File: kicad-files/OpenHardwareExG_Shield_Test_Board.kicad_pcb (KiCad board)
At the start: 4 copper layers, 125.1 x 59.7 mm, 150 parts, among them P1 CONN_1, P11 CONN_1, P12 CONN_1, P13 CONN_1, P14 CONN_1, P15 CONN_1, P16 CONN_1, P17 CONN_1, P18 CONN_1, P19 ARDUINO_SHIELD, P2 CONN_1, P23 CONN_1, P24 CONN_1, P25 CONN_1, P26 CONN_1, P27 CONN_1, P28 CONN_1, P29 CONN_1, P3 CONN_1, P30 CONN_1, P31 CONN_1, P32 CONN_1, P33 CONN_1, P34 CONN_1, P35 CONN_1, P36 CONN_1, P37 CONN_1, P38 CONN_1, P39 CONN_1, P4 CONN_1, P40 CONN_1, P41 CONN_1, P42 CONN_1, P43 CONN_1, P44 CONN_1, P45 CONN_1, P46 CONN_1, P47 CONN_1, P48 CONN_1, P49 CONN_1, P5 CONN_1, P50 CONN_1, P51 CONN_1, P52 CONN_1, P53 CONN_1, P54 CONN_1, P55 CONN_1, P56 CONN_3X2, P57 CONN_20X2, P6 CONN_1, P7 CONN_1, P8 CONN_1, P9 CONN_1, SW1 SW_PUSH, U1 74HC165, U2 74HC165, U3 74HC595PWR, U4 74HC165, U5 74LS125, U6 TPS2095D, U7 ADUM6000, U8 SI8661

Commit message: untangle the rats nest some
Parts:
- removed R45, R46, R47, R48, R49, R50: 47, SM0603
- moved R34 153.6 mm to (88.3, 55.9), turned to 270 degrees
- moved R39 152.5 mm to (87.6, 60.3), turned to 90 degrees
- moved R37 150.6 mm to (87.6, 64.8), turned to 270 degrees
- moved R36 147.1 mm to (88.3, 51.4), turned to 270 degrees
- moved R35 146.4 mm to (87.6, 68.6), turned to 270 degrees
- moved L1 144.1 mm to (89.5, 71.8), turned to 180 degrees
- moved R14 143.2 mm to (99.7, 62.2), turned to 90 degrees
- moved R12 142.2 mm to (99.7, 66.0), turned to 270 degrees
- moved R9 140.6 mm to (101.0, 52.7)
- moved L2 138.5 mm to (102.9, 71.8), turned to 90 degrees
- moved R11 138.1 mm to (101.0, 50.8)
- moved R13 137.9 mm to (101.0, 48.9)
- moved R15 137.1 mm to (101.0, 47.0)
- moved R10 136.7 mm to (104.8, 66.0)
- moved C5 136.2 mm to (105.4, 71.8), turned to 90 degrees
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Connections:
- net N-000001 renamed /A3
- net N-00000100 renamed /LED2
- net N-00000115 renamed /3.3V_BOGUS_ISO_DATA
- net N-00000132 renamed /LED1
- net N-00000136 renamed /VCC_DATA
- net N-0000018 renamed /A1
- net N-0000019 renamed /A2
- net N-000003 renamed /A4
- net N-0000040 renamed /VISO_BOGUS_ISO_PRE
- net N-0000043 renamed /MIDDLE_CARRY
- net N-0000045 renamed /VDD1
- net N-0000099 renamed /LED3
- U8 pad 11: N-0000020 -> /SHIFT_CLK_BOGUS_ISO
- U8 pad 12: N-0000021 -> /SHIFT_SH_~LD~_BOGUS_ISO
- U8 pad 13: N-0000035 -> /~SEND_TO_GND~_MASTER_BOGUS_ISO
- U8 pad 14: N-0000036 -> /SIGNAL_B_BOGUS_ISO
- U8 pad 15: N-0000022 -> /SIGNAL_A_BOGUS_ISO
- U8 pad 7: N-0000034 -> /SHIFT_CARRY
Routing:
- net /BIASOUT_FILT: track 0.00 -> 119.6 mm
- net /3.3V_BOGUS_ISO: track 0.00 -> 20.6 mm
- net /BIASINV: track 0.00 -> 13.5 mm
- net /SIGNAL_A_LADDER: track 0.00 -> 13.4 mm, vias 0 -> 1
- added copper zone on B.Cu, net GND
- added copper zone on F.Cu, net VCC

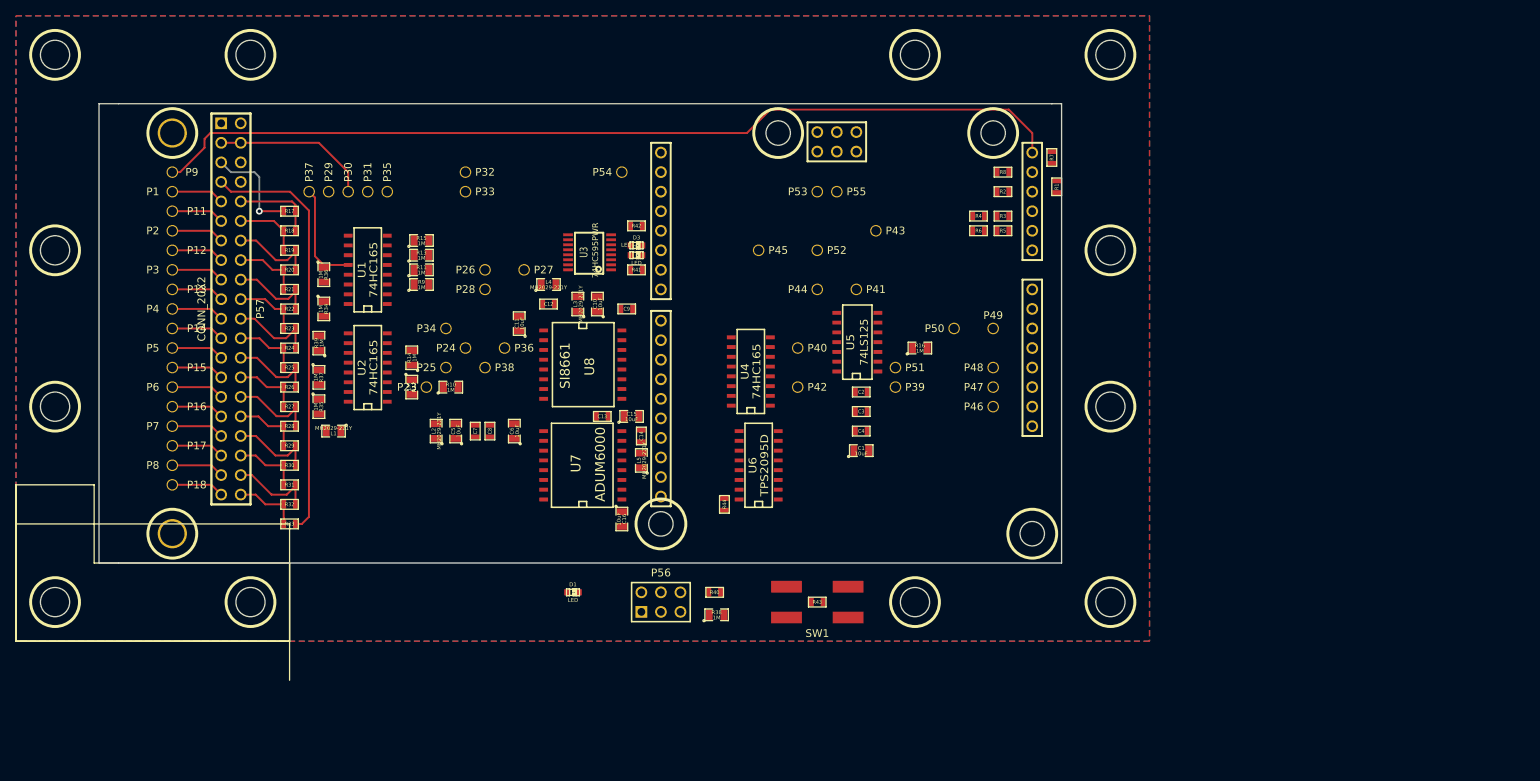
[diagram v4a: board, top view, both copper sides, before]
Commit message: move connectors onto .1 grid
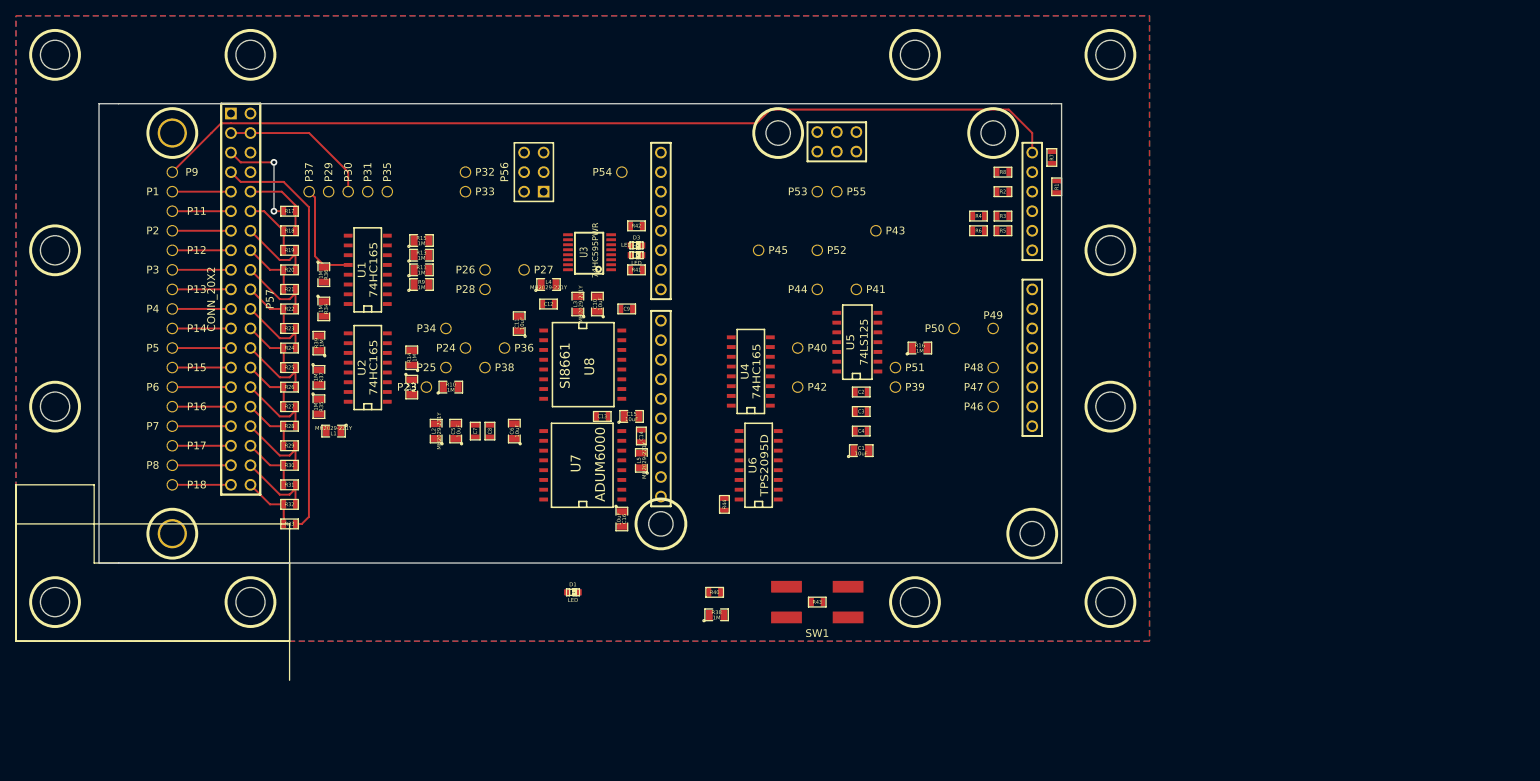
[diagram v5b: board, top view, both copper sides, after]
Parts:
- moved P56 58.3 mm to (115.6, 38.1), turned to 90 degrees
- moved P57 1.80 mm to (77.5, 54.6)
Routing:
- net /IN8N_LADDER: track 10.7 -> 9.88 mm
- net /IN8N: track 6.88 -> 7.62 mm
- net /IN6P_LADDER: track 8.65 -> 7.91 mm
- net /IN6P: track 6.88 -> 7.62 mm
- net /IN5P_LADDER: track 8.65 -> 7.91 mm
- net /IN5P: track 6.88 -> 7.62 mm
- net /IN5N: track 6.88 -> 7.62 mm
- net /IN4P_LADDER: track 8.65 -> 7.91 mm
- net /IN4P: track 6.88 -> 7.62 mm
- net /IN4N: track 6.88 -> 7.62 mm
- net /IN3P_LADDER: track 8.65 -> 7.91 mm
- net /IN3P: track 6.88 -> 7.62 mm
- net /IN3N: track 6.88 -> 7.62 mm
- net /IN2N: track 6.88 -> 7.62 mm
- net /IN1N: track 6.88 -> 7.62 mm
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
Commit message: power chips on isolated side of test harness from the board under test
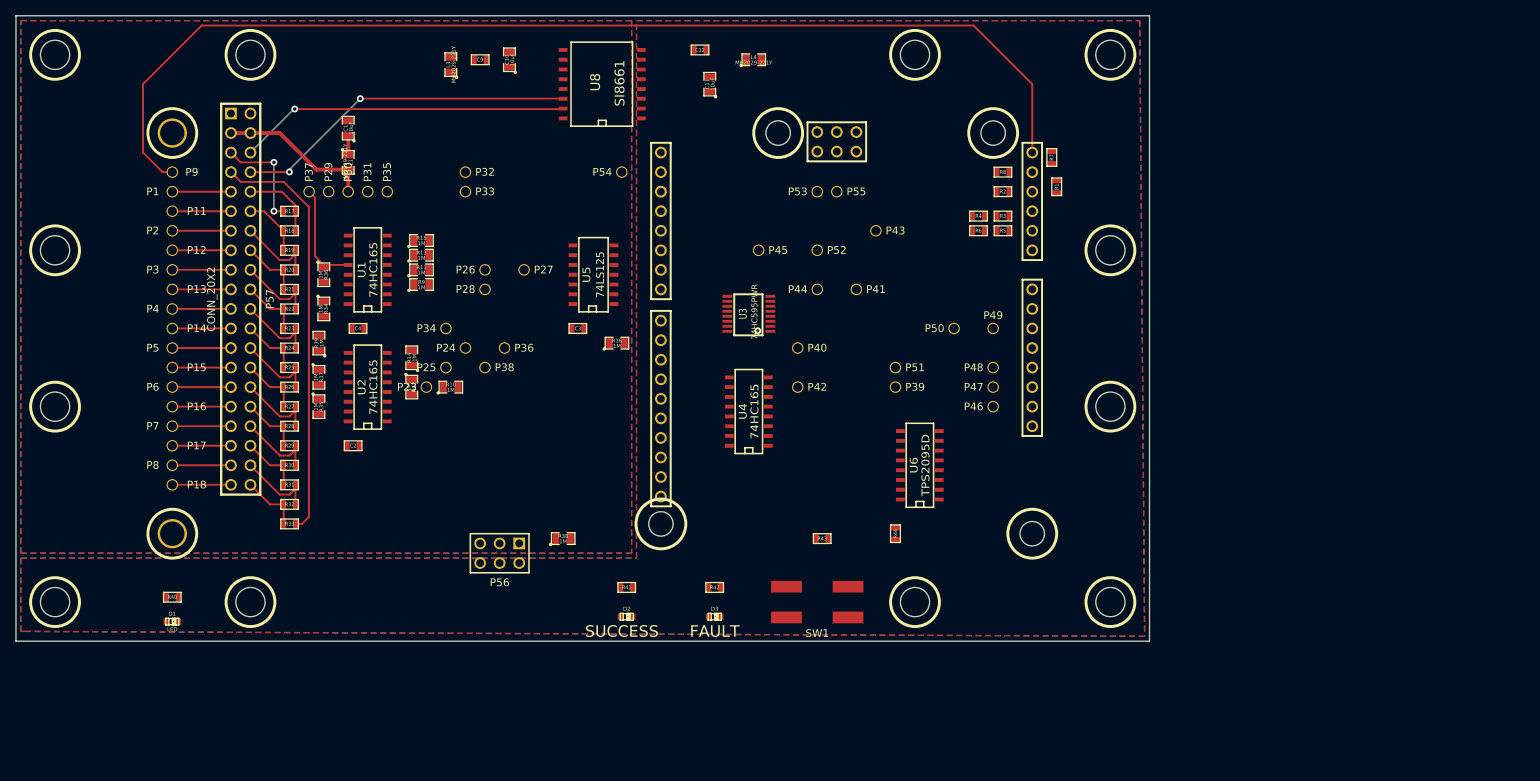
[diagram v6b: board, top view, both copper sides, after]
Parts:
- removed C13, C14, C7, C8: 100nF, SM0603
- removed C15, C16, C5, C6: 10uF, SM0805
- removed L2, L5: MH2029-221Y, SM0805
- removed U7: ADUM6000, SO16W
- moved C1 78.8 mm to (91.4, 32.4), turned to 90 degrees
- moved R40 70.5 mm to (68.6, 93.3)
- moved C4 66.8 mm to (92.7, 58.4)
- moved C2 66.4 mm to (92.1, 73.7)
- moved D1 52.2 mm to (68.6, 96.5)
- moved P56 49.7 mm to (111.1, 87.6), turned to 180 degrees
- moved D3 49.3 mm to (139.1, 95.9)
- moved R42 48.1 mm to (139.1, 92.1)
- moved D2 47.0 mm to (127.6, 95.9)
- moved R41 41.3 mm to (127.6, 92.1)
- moved C11 39.8 mm to (138.4, 26.7)
- moved L4 39.6 mm to (144.1, 23.5)
- moved R16 39.4 mm to (126.4, 60.3)
- moved C12 38.4 mm to (137.2, 22.2)
- moved C3 38.4 mm to (121.3, 58.4)
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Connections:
- L3 pad 2: /3.3V_BOGUS_ISO -> VCC
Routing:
- net /SIGNAL_B_BOGUS_ISO: track 0.00 -> 44.8 mm, vias 0 -> 2
- net /SIGNAL_A_BOGUS_ISO: track 0.00 -> 43.0 mm, vias 0 -> 1
- net /BIASOUT_FILT: track 118.9 -> 144.5 mm
- net VCC: track 0.00 -> 2.54 mm
- added copper zone on F.Cu, net /ARDUINO_VCC
- added copper zone on B.Cu, net GNDPWR
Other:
- board size 125.1 x 59.7 mm -> 147.3 x 81.3 mm
- board text added: "FAULT"
- board text added: "SUCCESS"

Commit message: routing of test harness half done
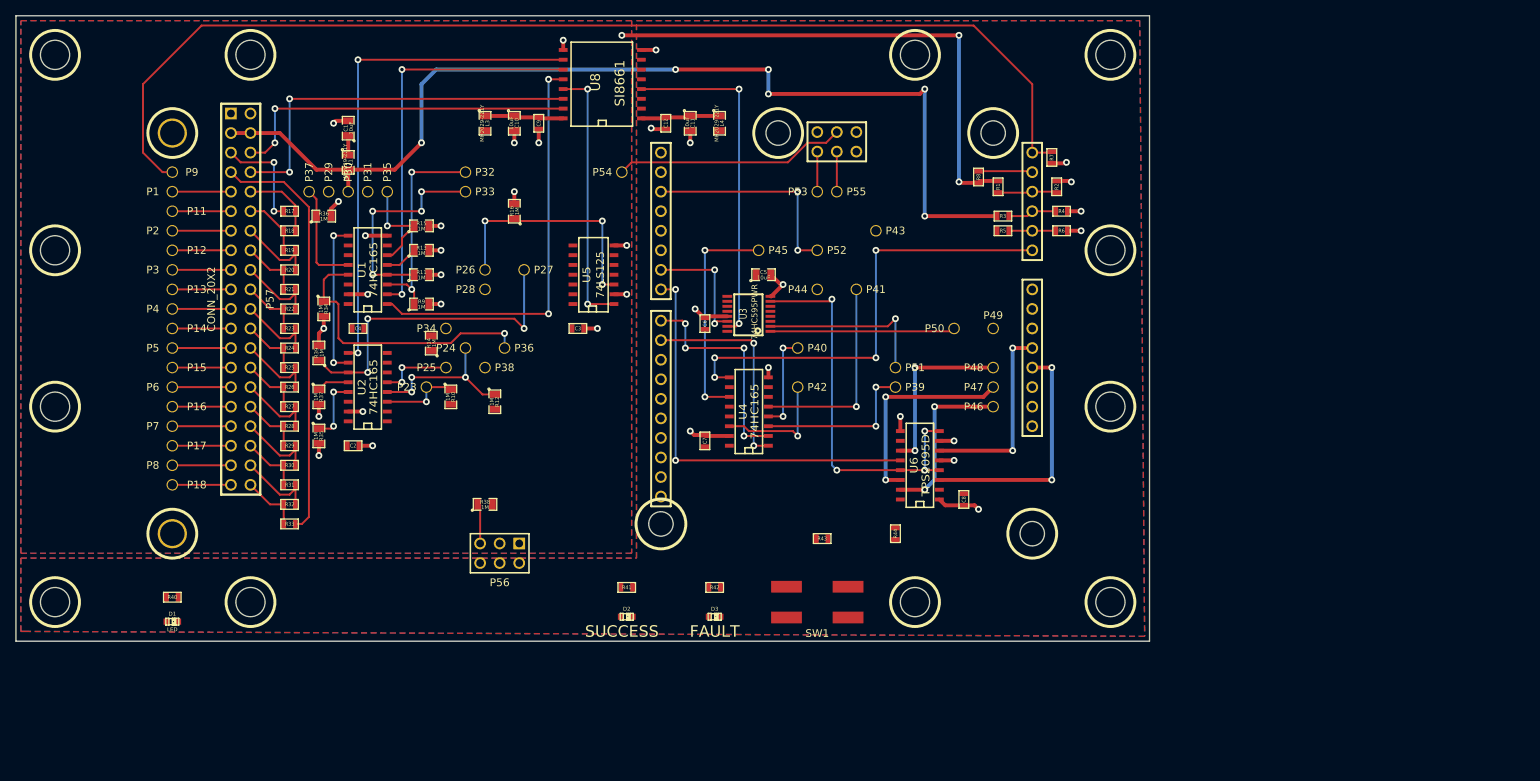
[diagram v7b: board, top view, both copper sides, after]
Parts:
- added C5: 10uF, SM0805, F.Cu at (145.4, 51.4)
- added C6: 100nF, SM0603, F.Cu at (137.8, 57.8)
- added C7: 100nF, SM0603, F.Cu at (137.8, 73.0)
- added C8: 100nF, SM0603, F.Cu at (171.4, 80.6)
- moved R16 21.7 mm to (113.0, 43.2), turned to 90 degrees
- moved C9 11.2 mm to (116.2, 31.8), turned to 270 degrees
- moved R38 11.1 mm to (109.2, 81.3)
- moved R12 11.0 mm to (110.5, 67.9)
- moved R4 10.8 mm to (184.2, 43.2)
- moved R6 10.8 mm to (184.2, 45.7)
- moved C12 10.5 mm to (132.7, 31.8), turned to 270 degrees
- moved L4 9.38 mm to (139.7, 31.8), turned to 270 degrees
- moved L3 8.82 mm to (109.2, 31.8), turned to 270 degrees
- moved C10 8.28 mm to (113.0, 31.8), turned to 270 degrees
- moved R36 7.62 mm to (88.3, 43.8), turned to 0 degrees
- moved R1 7.62 mm to (175.9, 40.0)
- moved R2 7.01 mm to (183.5, 40.0), turned to 90 degrees
- moved C11 5.68 mm to (135.9, 31.8), turned to 270 degrees
- moved R35 3.81 mm to (87.6, 72.4)
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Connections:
- P31 pad 1: /DGND_BOGUS_ISO -> GND
- R1 pad 1: /DGND_BOGUS_ISO -> GND
- R8 pad 1: /DGND_BOGUS_ISO -> GND
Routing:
- net /3.3V_BOGUS_ISO: track 20.1 -> 134.2 mm, vias 0 -> 6
- net GND: track 0.00 -> 106.4 mm, vias 0 -> 23
- net /SHIFT_CARRY_BOGUS_ISO: track 0.00 -> 66.0 mm, vias 0 -> 2
- net /SHIFT_IN: track 0.00 -> 59.7 mm, vias 0 -> 4
- net /SHIFT_SH_~LD~_BOGUS_ISO: track 0.00 -> 53.9 mm, vias 0 -> 2
- net /~SHIELD_SHORTED~: track 0.00 -> 53.3 mm, vias 0 -> 2
- net /SHIFT_CLK_BOGUS_ISO: track 0.00 -> 52.1 mm, vias 0 -> 2
- net /ENABLE_SHIELD: track 0.00 -> 50.9 mm, vias 0 -> 4
- net /~SEND_TO_GND~_MASTER: track 0.00 -> 44.9 mm, vias 0 -> 2
- net /ADS129x_DOUT_BOGUS_ISO: track 0.00 -> 42.5 mm, vias 0 -> 3
- net GNDPWR: track 0.00 -> 40.0 mm, vias 0 -> 15
- net /ADS129x_DAISY_IN_BOGUS_ISO: track 0.00 -> 37.1 mm, vias 0 -> 1
- net /MASTER_BOGUS_ISO: track 0.00 -> 35.3 mm, vias 0 -> 3
- net /~SEND_TO_GND~_MASTER_BOGUS_ISO: track 0.00 -> 34.5 mm, vias 0 -> 2
- net +3.3V: track 0.00 -> 31.7 mm, vias 0 -> 2
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
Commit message: finish initial routing of the test board
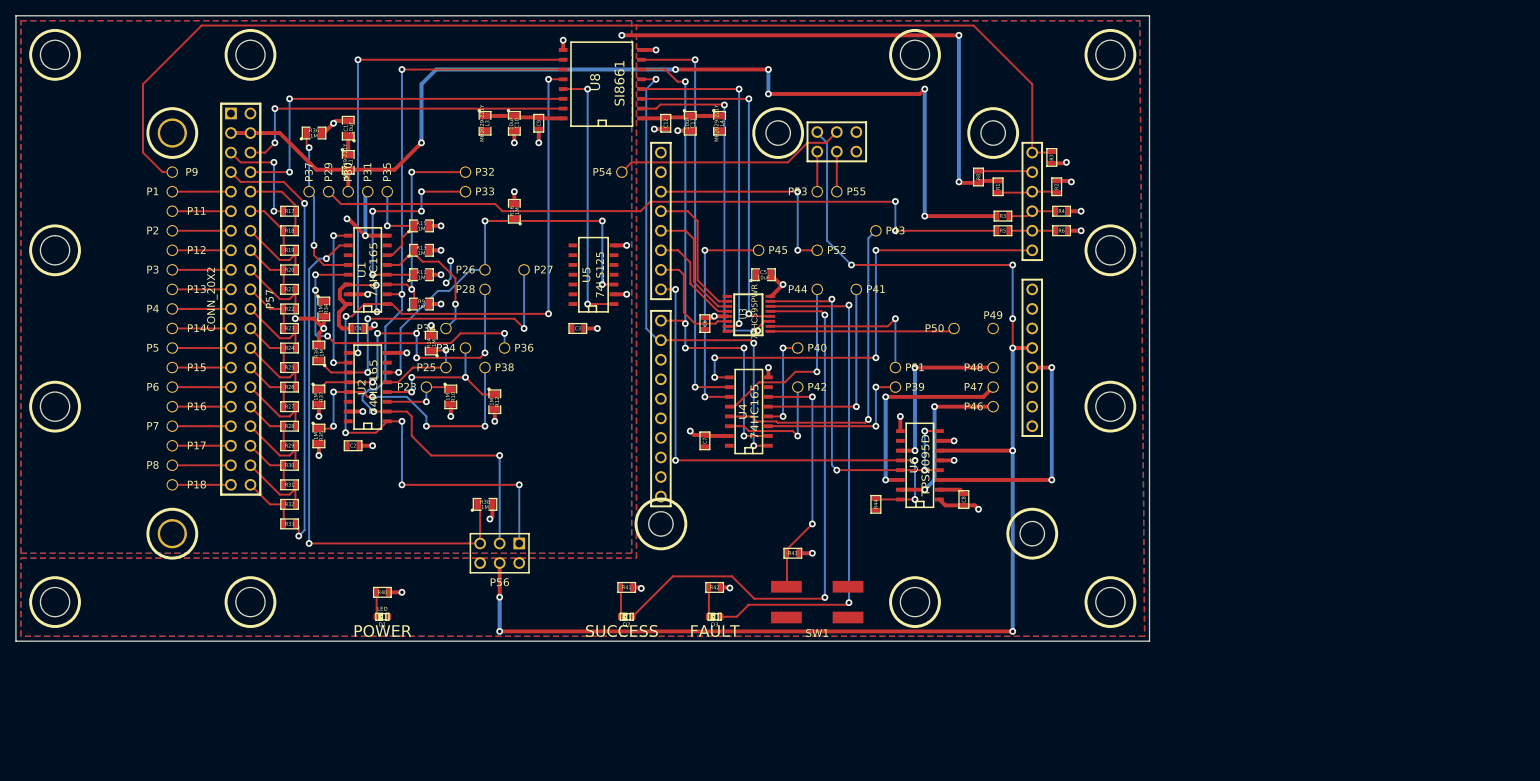
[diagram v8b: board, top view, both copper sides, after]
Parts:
- moved D1 27.3 mm to (95.9, 95.9), turned to 180 degrees
- moved R40 27.3 mm to (95.9, 92.7), turned to 0 degrees
- moved R36 10.9 mm to (87.0, 33.0)
- moved R44 4.58 mm to (160.0, 81.3)
- moved R43 4.26 mm to (149.2, 87.6)
- turned D2 to 180 degrees
- turned D3 to 180 degrees
- turned R41 to 0 degrees
- turned R42 to 0 degrees
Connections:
- R43 pad 2: GND -> GNDPWR
- SW1 pad 2: /3.3V_BOGUS_ISO -> /ARDUINO_VCC
- U1 pad 11: /3.3V_BOGUS_ISO -> VCC
- U1 pad 14: /3.3V_BOGUS_ISO -> VCC
- U2 pad 14: /3.3V_BOGUS_ISO -> VCC
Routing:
- net +5V: track 25.4 -> 175.3 mm, vias 2 -> 8
- net /VIN_BOGUS_ISO: track 0.00 -> 92.2 mm, vias 0 -> 2
- net /SUCCESS_LED: track 0.00 -> 72.4 mm, vias 0 -> 2
- net /FAULT_LED: track 0.00 -> 66.5 mm, vias 0 -> 2
- net /SHIFT_EXT_CARRY_BOGUS_ISO: track 5.21 -> 69.4 mm, vias 0 -> 2
- net /SHIFT_SH_~LD~_BOGUS_ISO: track 53.9 -> 114.1 mm, vias 2 -> 7
- net /SHIFT_CARRY: track 0.00 -> 54.0 mm, vias 0 -> 2
- net /SHIFT_CLK_BOGUS_ISO: track 52.1 -> 102.2 mm, vias 2 -> 4
- net /SIGNAL_A: track 0.00 -> 46.9 mm, vias 0 -> 2
- net /SIGNAL_B: track 0.00 -> 44.8 mm, vias 0 -> 2
- net /MASTER: track 0.00 -> 43.5 mm, vias 0 -> 1
- net /SHIFT_CLK: track 28.7 -> 66.5 mm, vias 4 -> 5
- net /SHIFT_SH_~LD~: track 27.5 -> 64.8 mm, vias 2 -> 3
- net /ADS129x_~DRDY~_BOGUS_ISO: track 4.20 -> 39.7 mm, vias 0 -> 5
- net /GO_BUTTON: track 0.00 -> 31.8 mm, vias 0 -> 2
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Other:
- board text added: "POWER"
